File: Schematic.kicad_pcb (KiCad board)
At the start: 2 copper layers, 32 x 32 mm, 27 parts, among them J1 S2B-PH-K-S_LF__SN_, J2 Conn_01x04_Female, J3 Conn_02x05_Odd_Even, J4 Conn_01x05_Female, Q1 BSS138, Q2 BSS138, Q3 BSS138, U1 U1, U2 AP7333-33SAG

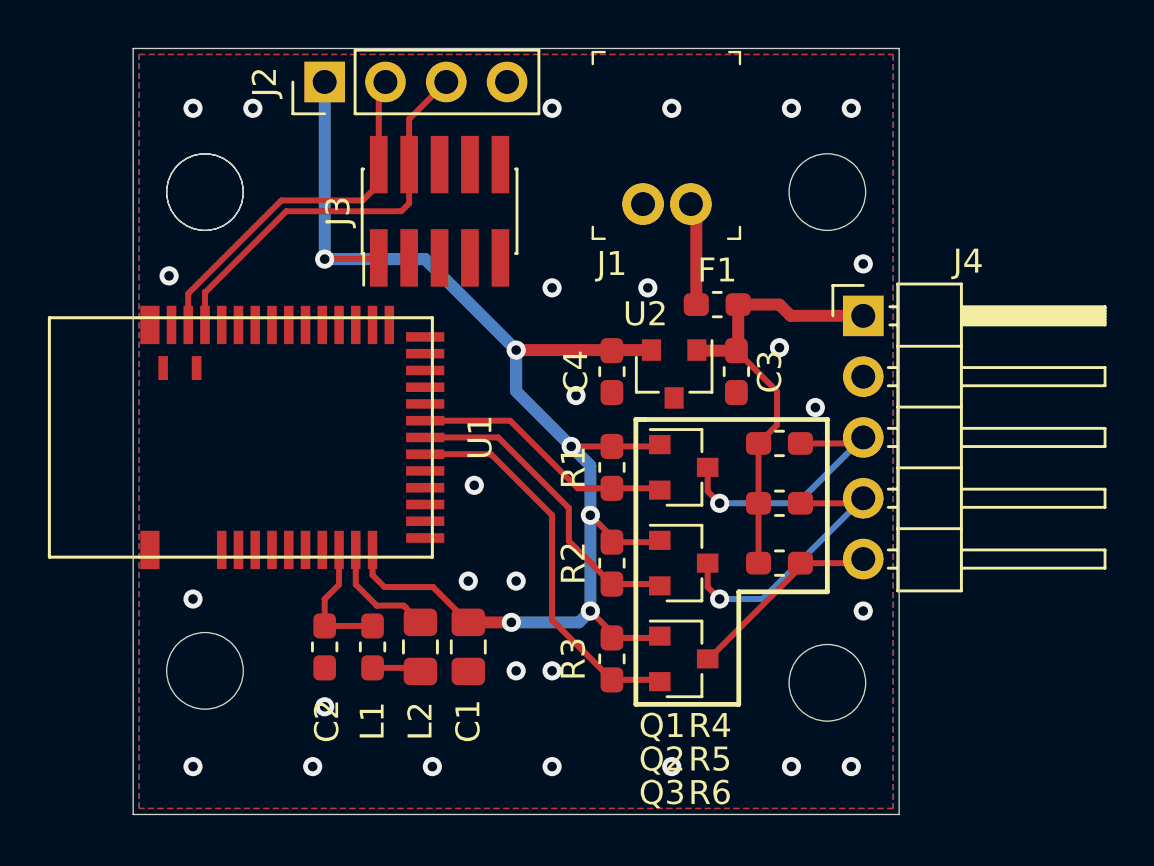
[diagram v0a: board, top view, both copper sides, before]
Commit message: TP等を追加
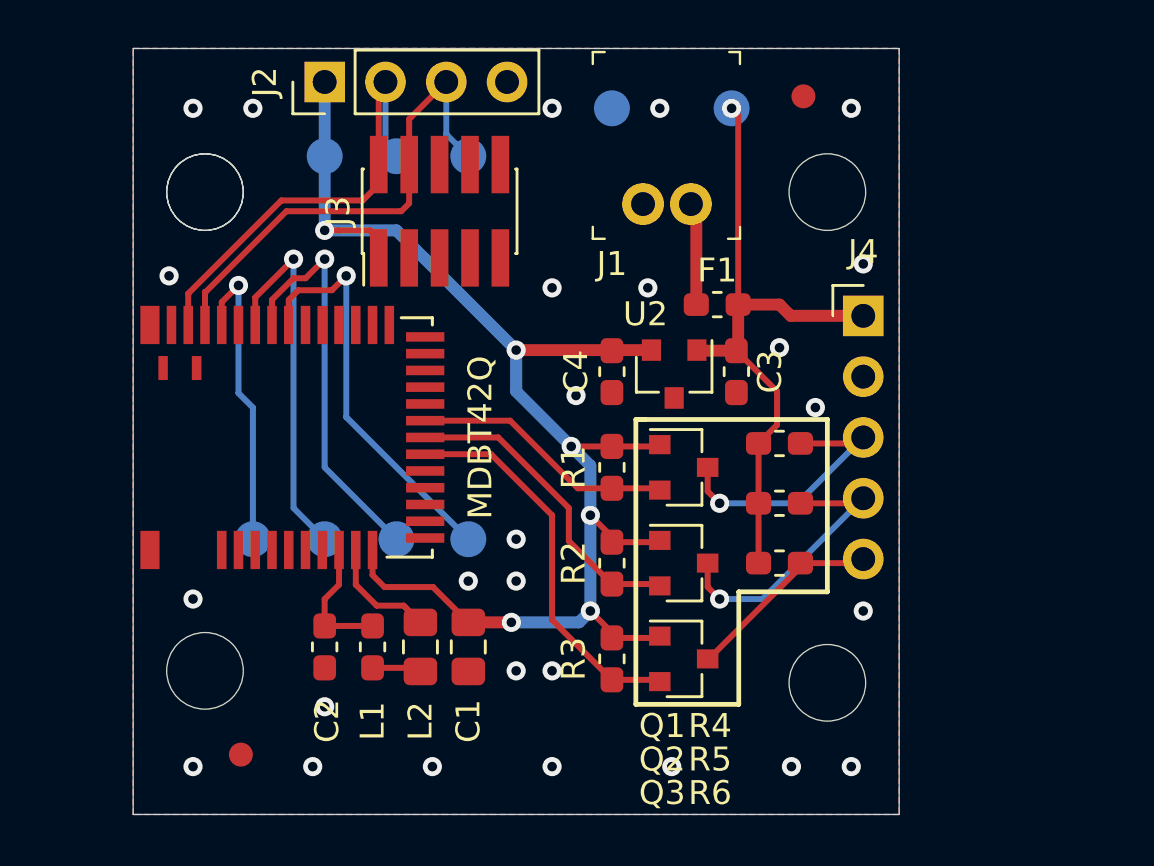
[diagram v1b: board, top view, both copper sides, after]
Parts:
- added REF**: Fiducial_1mm_Mask2mm, Fiducial:Fiducial_1mm_Mask2mm, F.Cu at (118.0, 62.0)
- added REF**: Fiducial_1mm_Mask2mm, Fiducial:Fiducial_1mm_Mask2mm, F.Cu at (94.5, 89.5)
- added TP1: TestPoint, TestPoint:TestPoint_Pad_D1.5mm, B.Cu at (115.0, 62.5)
- added TP2: TestPoint, TestPoint:TestPoint_Pad_D1.5mm, B.Cu at (98.0, 64.5)
- added TP3: TestPoint, TestPoint:TestPoint_Pad_D1.5mm, B.Cu at (110.0, 62.5)
- added TP4: TestPoint, TestPoint:TestPoint_Pad_D1.5mm, B.Cu at (101.0, 64.5)
- added TP5: TestPoint, TestPoint:TestPoint_Pad_D1.5mm, B.Cu at (104.0, 64.5)
- added TP6: TestPoint, TestPoint:TestPoint_Pad_D1.5mm, B.Cu at (95.0, 80.5)
- added TP7: TestPoint, TestPoint:TestPoint_Pad_D1.5mm, B.Cu at (98.0, 80.5)
- added TP8: TestPoint, TestPoint:TestPoint_Pad_D1.5mm, B.Cu at (101.0, 80.5)
- added TP9: TestPoint, TestPoint:TestPoint_Pad_D1.5mm, B.Cu at (104.0, 80.5)
- U1: value U1 -> MDBT42Q
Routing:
- net /UART_RX: track 0.00 -> 17.0 mm, vias 0 -> 1
- net /UART_RTS: track 0.00 -> 16.9 mm, vias 0 -> 1
- net /UART_CTS: track 0.00 -> 15.7 mm, vias 0 -> 1
- net /UART_TX: track 0.00 -> 12.8 mm, vias 0 -> 1
- net +BATT: track 18.9 -> 27.3 mm, vias 0 -> 1
- net /SWDCLK: track 17.2 -> 20.6 mm
- net /SWDIO: track 15.6 -> 18.8 mm
- net GND: vias 28 -> 27
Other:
- board text added: "CTS"
- board text added: "NoraHACK BLE-LED Board"
- board text added: "RTS"
- board text added: "RX"
- board text added: "TX"
